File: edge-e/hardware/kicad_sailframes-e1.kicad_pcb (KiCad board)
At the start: 2 copper layers, 76.5 x 111 mm, 6 parts, among them J1 Conn_01x06, J2 Conn_01x04, J3 Conn_01x10, J4 Conn_01x04, J5 Conn_01x02

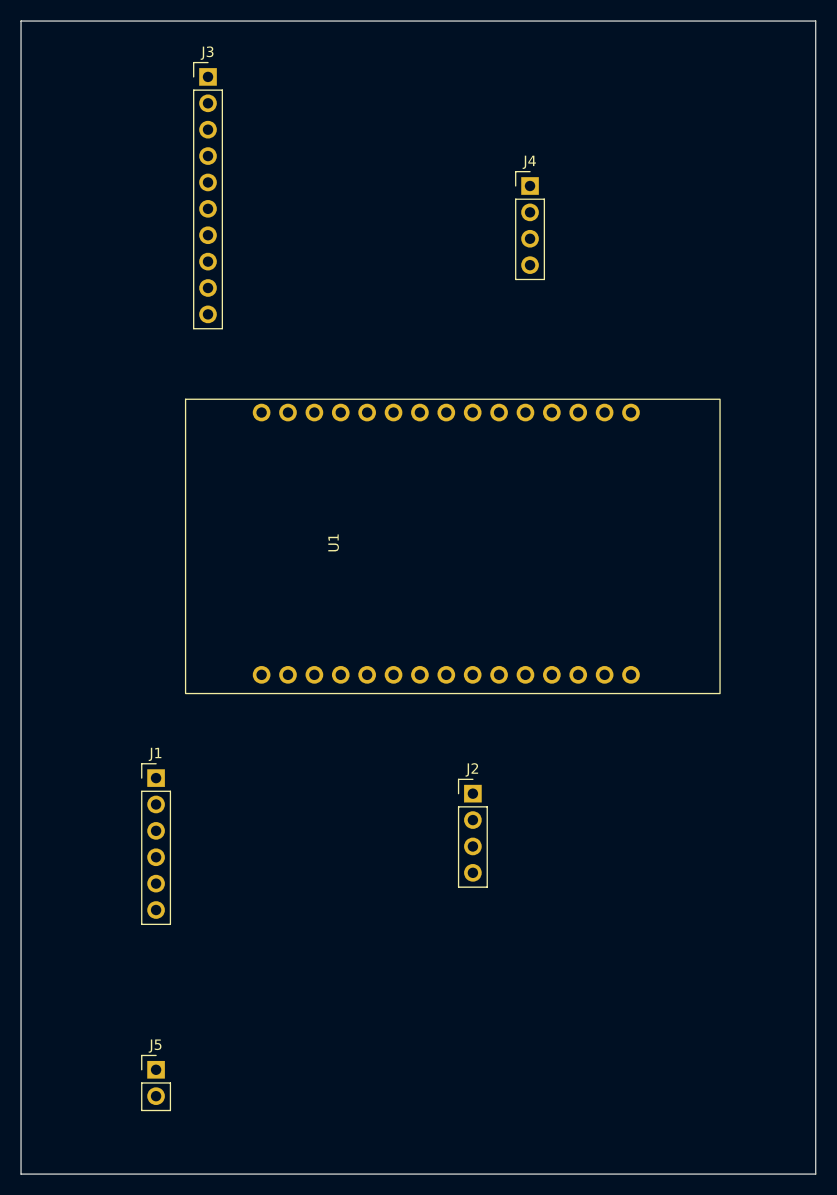
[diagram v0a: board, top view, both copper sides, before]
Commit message: E1 PCB v1.0: complete KiCad design with TFT display
Hardware changes:
- Replace OLED with Hosyond 3.5 TFT ST7796U for sunlight readability
- TFT on VSPI bus, SD card on HSPI bus - eliminates display flicker
- Replace PowerBoost 1000C with DWEII USB-C boost charger
- Add 6000mAh LiPo battery with JST PH 2.0mm connector
- Battery voltage divider: 2x 100K for ADC monitoring

PCB design:
- 60.5 x 91.5mm, 2-layer board
- Connectors: GPS, IMU, TFT, SD, battery, power switch
- Expansion: Wind sensor UART1, I2C headers, GPIO expansion
- Ground pour on bottom layer
- Gerbers generated and ordered from JLCPCB

Pin swaps in User_Setup.h to match soldered prototype:
- TFT_MISO: GPIO19 to GPIO25
- TFT_BL: GPIO25 to GPIO19

Co-Authored-By: Claude Opus 4.5 <noreply@anthropic.com>
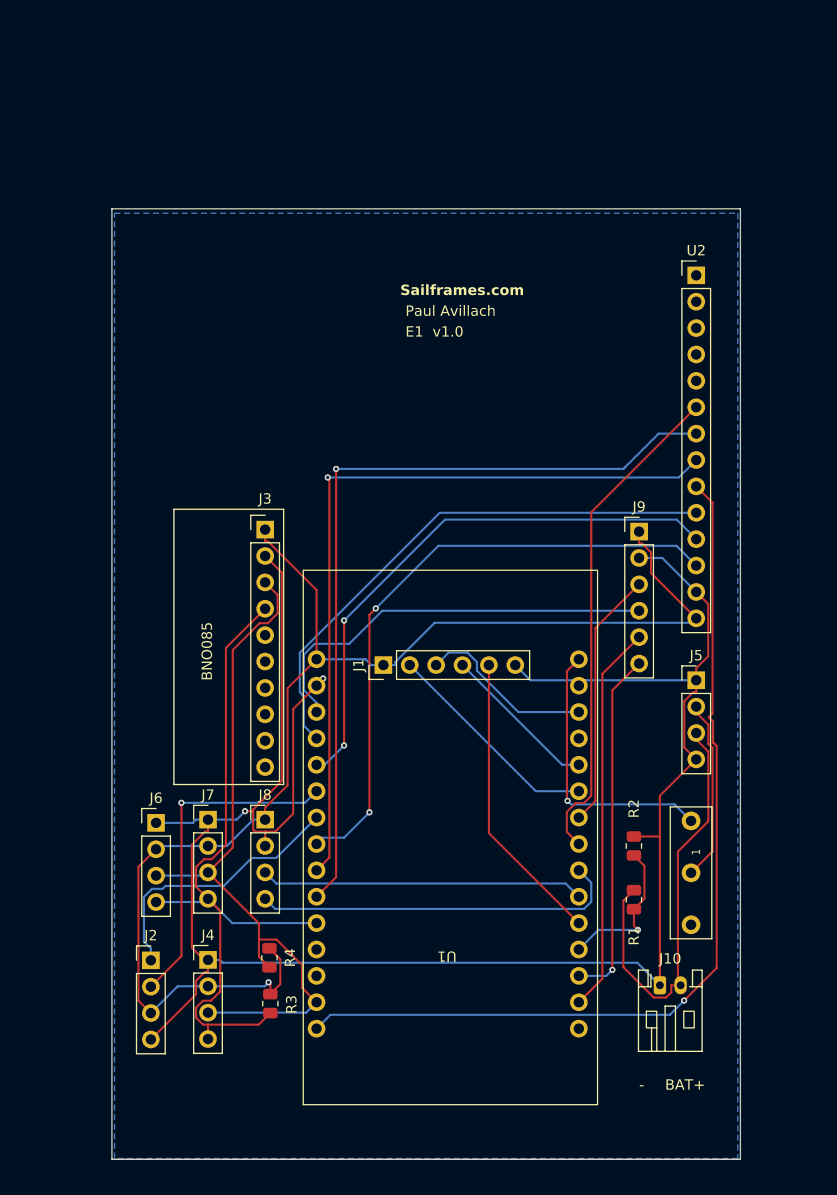
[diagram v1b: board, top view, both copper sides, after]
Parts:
- added J10: Conn_01x02, Connector_JST:JST_PH_S2B-PH-K_1x02_P2.00mm_Horizontal, F.Cu at (160.0, 125.3)
- added J6: Conn_01x04, Connector_PinHeader_2.54mm:PinHeader_1x04_P2.54mm_Vertical, F.Cu at (111.5, 109.7)
- added J7: Conn_01x04, Connector_PinHeader_2.54mm:PinHeader_1x04_P2.54mm_Vertical, F.Cu at (116.5, 109.4)
- added J8: Conn_01x04, Connector_PinHeader_2.54mm:PinHeader_1x04_P2.54mm_Vertical, F.Cu at (122.0, 109.4)
- added J9: Conn_01x06, Connector_PinHeader_2.54mm:PinHeader_1x06_P2.54mm_Vertical, F.Cu at (158.0, 81.7)
- added R1: 100K, Resistor_SMD:R_0805_2012Metric, F.Cu at (157.5, 117.1)
- added R2: 100K, Resistor_SMD:R_0805_2012Metric, F.Cu at (157.5, 111.9)
- added R3: 4.7K, Resistor_SMD:R_0805_2012Metric, F.Cu at (122.5, 127.1)
- added R4: 4.7K, Resistor_SMD:R_0805_2012Metric, F.Cu at (122.4, 122.7)
- added SW1: SW_SPDT, esp32devkitv1:SW_Slide_SPDT_SS12D10-G5_P5mm, F.Cu at (163.0, 114.5)
- added U2: Hosyond_3.5_ST7796U, Connector_PinHeader_2.54mm:PinHeader_1x14_P2.54mm_Vertical, F.Cu at (163.5, 57.0)
- J5: value Conn_01x02 -> Conn_01x04; footprint Connector_PinHeader_2.54mm:PinHeader_1x02_P2.54mm_Vertical -> Connector_PinHeader_2.54mm:PinHeader_1x04_P2.54mm_Vertical
- moved J4 80.7 mm to (116.5, 122.9)
- moved J5 64.1 mm to (163.5, 96.0)
- moved U1 45.7 mm to (152.2, 129.5), turned to 90 degrees
- moved J3 43.9 mm to (122.0, 81.5)
- moved J2 34.9 mm to (111.0, 122.9)
- moved J1 24.4 mm to (133.4, 94.5), turned to 90 degrees
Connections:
- net /SCL renamed /I2C_SCL
- net /SDA renamed /I2C_SDA
- J1 pad 2: /SD_CS -> /HSPI_CS
- J1 pad 3: /MOSI -> /HSPI_MOSI
- J1 pad 4: /SCK -> /HSPI_CLK
- J1 pad 5: /MISO -> /HSPI_MISO
- J2 pad 1: /GPS_TX -> /GPS_RX3
- J2 pad 2: /GPS_RX -> /GPS_TX3
- J2 pad 3: /5V_IN -> /3V3
- J5 pad 1: /5V_IN -> /GND
- J5 pad 2: /GND -> /SW_5V_IN
- U1 pad 10: unconnected-(U1-D27-Pad10) -> /HSPI_CS
- U1 pad 11: unconnected-(U1-D14-Pad11) -> /HSPI_CLK
- U1 pad 13: unconnected-(U1-D13-Pad13) -> /HSPI_MOSI
- U1 pad 18: unconnected-(U1-D15-Pad18) -> /D15
- U1 pad 19: unconnected-(U1-D2-Pad19) -> /TFT_DC
- U1 pad 2: unconnected-(U1-VP-Pad2) -> /VP
- U1 pad 20: unconnected-(U1-D4-Pad20) -> /TFT_RST
- U1 pad 21: /GPS_TX -> /GPS_TX3
- U1 pad 22: /GPS_RX -> /GPS_RX3
- U1 pad 23: /SD_CS -> /TFT_CS
- U1 pad 24: /SCK -> /VSPI_CLK
- U1 pad 25: /MISO -> /TFT_BL
- U1 pad 3: unconnected-(U1-VN-Pad3) -> /VN
- U1 pad 30: /MOSI -> /VSPI_MOSI
- U1 pad 4: unconnected-(U1-D34-Pad4) -> /VBAT_DIV
- U1 pad 5: unconnected-(U1-D35-Pad5) -> /HSPI_MISO
- U1 pad 6: unconnected-(U1-D32-Pad6) -> /WIND_TX
- U1 pad 7: unconnected-(U1-D33-Pad7) -> /WIND_RX
- U1 pad 8: unconnected-(U1-D25-Pad8) -> /VSPI_MISO
- U1 pad 9: unconnected-(U1-D26-Pad9) -> /D26
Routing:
- net /GND: track 0.00 -> 198.6 mm, vias 0 -> 2
- net /3V3: track 0.00 -> 129.4 mm, vias 0 -> 1
- net /VSPI_MOSI: track 0.00 -> 88.8 mm, vias 0 -> 1
- net /TFT_BL: track 0.00 -> 78.3 mm, vias 0 -> 1
- net /VSPI_CLK: track 0.00 -> 74.6 mm, vias 0 -> 1
- net /I2C_SDA: track 0.00 -> 70.8 mm
- net /I2C_SCL: track 0.00 -> 68.6 mm
- net /TFT_CS: track 0.00 -> 60.4 mm, vias 0 -> 2
- net /TFT_RST: track 0.00 -> 54.2 mm, vias 0 -> 2
- net /TFT_DC: track 0.00 -> 52.9 mm
- net /VSPI_MISO: track 0.00 -> 48.1 mm
- net /VBAT: track 0.00 -> 41.4 mm
- net /D15: track 0.00 -> 40.1 mm
- net /VP: track 0.00 -> 37.6 mm
- net /WIND_RX: track 0.00 -> 35.6 mm
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- added copper zone on B.Cu, net /GND
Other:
- board size 76.5 x 111 mm -> 60.5 x 91.5 mm
- board text added: "-"
- board text added: "BAT+"
- board text added: "BNO085"
- board text added: "E1 v1.0"
- board text added: "Paul Avillach"
- board text added: "Sailframes.com"

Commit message: E1 PCB v1.1: add ground pour, mounting holes, and layout updates
Hardware:
- Add ground pour on B.Cu layer for improved EMI shielding
- Add 4x M2.5 mounting holes at corners
- Update PCB layout with component repositioning
- Add custom SPDT switch footprint (SS12D10-G5)
- Remove unused footprint libraries (DWEII, esp32devkitv1)
- Add BOM, Gerber job file, and Specctra DSN export

Firmware:
- Add E1 SD card config files (config.txt, imu_cal.txt, wind_mac.txt)

Web dashboard:
- Update chart panel and map view components
- CSS and layout improvements

Lambda/Scripts:
- Update PPK processing and upload handlers
- Add GPS reprocessing scripts (10Hz, timestamps, all sessions)
- Add session restore utility

Documentation:
- Add E1 display upgrade, firmware MSM, and power/battery specs
- Update LG290P configuration notes
- Add RTKLIB obs codes fix documentation

Co-Authored-By: Claude Opus 4.5 <noreply@anthropic.com>
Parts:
- added H1: MountingHole_2.7mm_M2.5, MountingHole:MountingHole_2.7mm_M2.5, F.Cu at (110.5, 54.0)
- added H2: MountingHole_2.7mm_M2.5, MountingHole:MountingHole_2.7mm_M2.5, F.Cu at (164.5, 53.5)
- added H3: MountingHole_2.7mm_M2.5, MountingHole:MountingHole_2.7mm_M2.5, F.Cu at (164.5, 139.0)
- added H4: MountingHole_2.7mm_M2.5, MountingHole:MountingHole_2.7mm_M2.5, F.Cu at (110.5, 138.5)
- SW1: footprint esp32devkitv1:SW_Slide_SPDT_SS12D10-G5_P5mm -> e1_Library:SW_Slide_SS12D10-G5_v3_SAILFRAMES
- moved U2 13.7 mm to (164.0, 70.6)
- moved J5 5.50 mm to (158.0, 96.0)
- moved J9 3.50 mm to (158.0, 78.2)
- moved SW1 0.50 mm to (163.5, 114.5)
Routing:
- net /3V3: track 129.4 -> 162.9 mm
- net /WIND_TX: track 31.2 -> 53.8 mm, vias 0 -> 1
- net /WIND_RX: track 35.6 -> 57.0 mm, vias 0 -> 1
- net /GND: track 198.6 -> 182.7 mm, vias 2 -> 0
- net /VSPI_MISO: track 48.1 -> 34.1 mm, vias 0 -> 1
- net /VSPI_CLK: track 74.6 -> 60.7 mm
- net /VSPI_MOSI: track 88.8 -> 76.4 mm
- net /TFT_BL: track 78.3 -> 68.2 mm, vias 1 -> 2
- net /VBAT: track 41.4 -> 33.3 mm
- net /TFT_DC: track 52.9 -> 45.4 mm
- net /TFT_RST: track 54.2 -> 48.0 mm, vias 2 -> 0
- net /I2C_SDA: track 70.8 -> 65.3 mm, vias 0 -> 2
- net /VN: track 34.0 -> 39.3 mm
- net /VP: track 37.6 -> 41.1 mm
- net /D26: track 24.9 -> 28.4 mm
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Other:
- board text added: "E1 to E10 v1.1"
- board text removed: "E1 v1.0"
